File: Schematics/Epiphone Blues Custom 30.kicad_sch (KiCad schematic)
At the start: 280 parts, among them J3 Conn_Coaxial_Power, M1 Fan, SW2 EQ mode, SW3 POWER, SW5 PENTODE

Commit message: changed color of master volume
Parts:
- added A1: Arduino_UNO_R2, Module:Arduino_UNO_R2, symbol MCU_Module:Arduino_UNO_R2
- added D15: D, symbol Device:D
- added J10: Midi In, symbol Connector:DIN-5_180degree
- added M2: Servo, symbol Motor:Motor_Servo
- added R39: 220R, symbol Device:R
- added R54: 470R, symbol Device:R
- added R55: 1K, symbol Device:R
- added U1: 6N138, symbol Isolator:6N138
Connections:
- net at FCR.: now also B., C33.1, R49.1; no longer TRF4.
- net at 0VAC.: now also TR2.; no longer PT3.
- net at 60VAC.: now also TR2.; no longer PT11.
- net at PT2.: now also PT3., PT6. (x2)
- net at V7.: now also C29.1, R44.2, V6.
- net at PT5.: now also PT6. (x2)
- net at PT6.: no longer PT5. (x2)
- net at PT4.: now also PT1., PT7.
- net at ff.: now also BLUE.; no longer TR3.
- net at BLUE.: now also OT6.; no longer ff.
- net at PT7.: now also PT1.
- net at PT1.: no longer PT7.
- net at U?.: now also OUT1.; no longer TR3.
- net at OUT1.: now also PS1., V6.; no longer U?.
- net at 120VAC.: now also TR2.; no longer PT5.
- net at TR3.: now also d.; no longer d.
- net at a.: now also d.; no longer TR3.
- net at s.: now also d.; no longer TR3.
- net at d.: now also s.; no longer TR3.
- net at PT7.: now also 100VAC.
- net at 100VAC.: now also TR2.; no longer PT7.
- net at 5VAC.: now also PT13.
- net at PT13.: now also C35.1, HTFS., R50.1, V8.; no longer 5VAC.
- net at BLK.: now also SW3.; no longer PT1.
- net at SW3.: now also BLU.; no longer BLK.
- net at 0VAC.: now also TR2.; no longer PT6.
- net at 100VAC.: now also TR2.; no longer PT4.
- net at V6., V7.: now also PT15.; no longer PT14.
- net at PT1.: now also PT8.
- net at PT8.: no longer PT1.
- net at SW2.: now also RV7.; no longer RV5.
- net at RV7.: now also R23.2; no longer SW2.
- net at 120VAC.: now also TR2.; no longer PT8.
- net at PT2.: now also PT3.
- net at PT3.: no longer PT2.
- net at PT5.: now also PT1., PT8.
- net at 0VAC.: now also PT12.
- net at PT12.: now also F7.1; no longer 0VAC.
- net at s.: now also a.; no longer d.
- net at a.: now also J6., J7.; no longer s.
- net at BRN.: now also F9.2; no longer SW3.
- net at BLU.: now also AC-Input1.; no longer SW3.
- net at PT3.: now also PT2.
- net at PT2.: no longer PT3.
- new net: D6.1 (K), D7.1 (K), F., M1. (-), V1., V2., V3., V4., V5.
- new net: FCR., TRF4.
- new net: 0VAC., PT3.
- new net: 0VAC., TR2. (x2)
- new net: D4.2 (A), J4., RL3.
- new net: D3.2 (A), J4., RL1., RLY2.
- new net: J4., PB1.
- new net: 60VAC., PT11.
- new net: J3. (In), R29.1, RL3., V5A., V5B.
- new net: OUT2., PS2., V7.
- new net: TR3., ff.
- new net: TR3., U?.
- new net: B., PS5., PS6.
- new net: J5., J6., J7., J8., J9., d.
- new net: C4.2, RLY2., RV1.
- new net: 120VAC., PT5.
- new net: R19.2, RLY2., V2B.
- new net: RLY2., RV4.
- new net: TR3., d.
- new net: TR3., a.
- new net: TR3., s.
- new net: A1.15 (D0/RX), M2.1 (PWM)
- new net: A1.29 (GND), M2.3 (-), R55.2, U1.5 (GND)
- new net: A1.5 (+5V), M2.2 (+), R54.1, U1.8 (VCC)
- new net: BLK., PT1.
- new net: 0VAC., PT6.
- new net: 100VAC., PT4.
- new net: PT14., V6., V7.
- new net: C17.2, RV7., SW2.
- new net: RV5., SW2.
- new net: 120VAC., PT8.
- new net: R54.2, U1.6 (VO2)
- new net: D15.1 (K), R39.2, U1.2 (C1)
- new net: D15.2 (A), J10.5, U1.3 (C2)
- new net: C6.2, RL1., RV2., V1B.
- new net: BRN., SW3.
- new net: J2. (Ext), T1. (SA)
- new net: J10.4, R39.1
- new net: R55.1, U1.7 (VO1)
- now unconnected: PT1., PT1., PT3., PT3., PT6., PT6., PT7., PT8., V6., V6.
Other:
- note added: "Master volume is controlled by a servo motor. A MIDI expression pedal defines the rotation"
- moved on the sheet: 0VAC, 100VAC, 11.5VAC, 120VAC, 3.15VAC, 350VAC, 5VAC, 60VAC, A, AC-Input1, B, BLK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

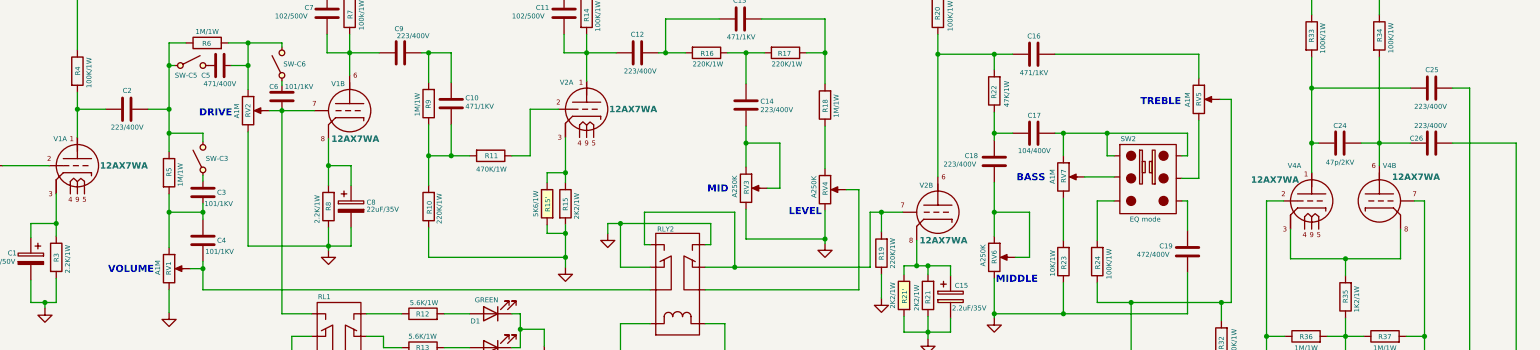
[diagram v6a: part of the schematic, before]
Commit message: Changed tube types in V1, V2 and V4
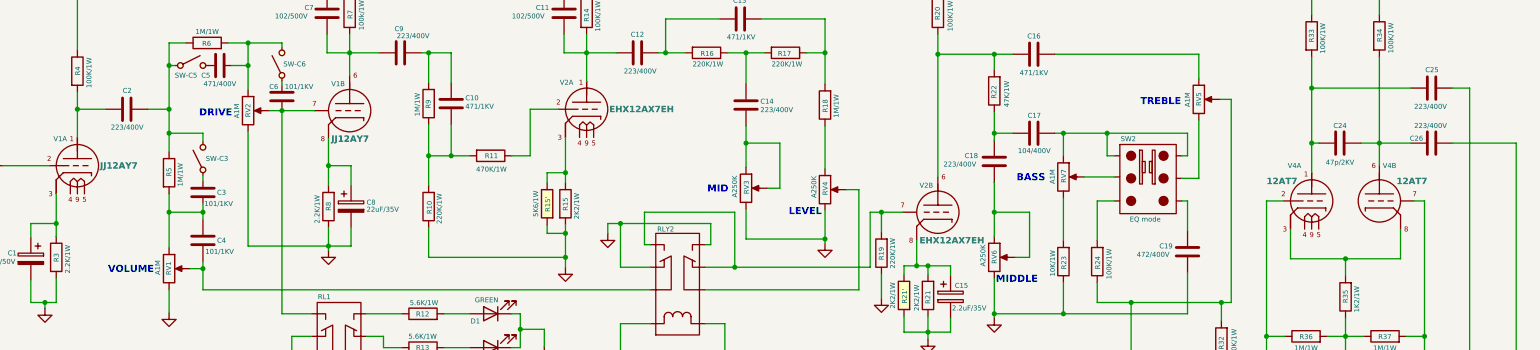
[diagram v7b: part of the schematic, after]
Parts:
- 0VAC, 100VAC, 11.5VAC, 120VAC, 3.15VAC, 350VAC, 5VAC, 60VAC, A, AC-Input1, B, BLK, BLU, BLUE, BRN, C, D, D10, D11, D12, D13, D14, D9, E, F, FCR, FCS, HTFR, HTFS, J1, J2, J4, J5, J6, J7, J8, J9, OTCT, OUT1, OUT2, PS1, PS2, PS3, PS4, PS5, PS6, PT1, PT10, PT11, PT12, PT13, PT14, PT15, PT2, PT3, PT4, PT5, PT6, PT7, PT8, PT9, RL1, RL3, RLY2, SS1, SS2, SW-C3, SW-C5, SW-C6, T1, V1, V2, V3, V4, V5, V6, V7, WHT: value ~ -> (none)
- V1A, V1B: value 12AX7WA -> JJ12AY7
- V2A, V2B: value 12AX7WA -> EHX12AX7EH
- V4A, V4B: value 12AX7WA -> 12AT7
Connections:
- net at FCR.: now also B., C33.1, R49.1; no longer TRF4.
- net at 0VAC.: now also TR2.; no longer PT3.
- net at 60VAC.: now also TR2.; no longer PT11.
- net at PT2.: now also PT3., PT6. (x2)
- net at V7.: now also C29.1, R44.2, V6.
- net at PT5.: now also PT6. (x2)
- net at PT6.: no longer PT5. (x2)
- net at PT4.: now also PT1., PT7.
- net at ff.: now also BLUE.; no longer TR3.
- net at BLUE.: now also OT6.; no longer ff.
- net at PT7.: now also PT1.
- net at PT1.: no longer PT7.
- net at U?.: now also OUT1.; no longer TR3.
- net at OUT1.: now also PS1., V6.; no longer U?.
- net at 120VAC.: now also TR2.; no longer PT5.
- net at TR3.: now also d.; no longer d.
- net at a.: now also d.; no longer TR3.
- net at s.: now also d.; no longer TR3.
- net at d.: now also s.; no longer TR3.
- net at PT7.: now also 100VAC.
- net at 100VAC.: now also TR2.; no longer PT7.
- net at 5VAC.: now also PT13.
- net at PT13.: now also C35.1, HTFS., R50.1, V8.; no longer 5VAC.
- net at BLK.: now also SW3.; no longer PT1.
- net at SW3.: now also BLU.; no longer BLK.
- net at 0VAC.: now also TR2.; no longer PT6.
- net at 100VAC.: now also TR2.; no longer PT4.
- net at V6., V7.: now also PT15.; no longer PT14.
- net at PT1.: now also PT8.
- net at PT8.: no longer PT1.
- net at SW2.: now also RV7.; no longer RV5.
- net at RV7.: now also R23.2; no longer SW2.
- net at 120VAC.: now also TR2.; no longer PT8.
- net at PT2.: now also PT3.
- net at PT3.: no longer PT2.
- net at PT5.: now also PT1., PT8.
- net at 0VAC.: now also PT12.
- net at PT12.: now also F7.1; no longer 0VAC.
- net at s.: now also a.; no longer d.
- net at a.: now also J6., J7.; no longer s.
- net at BRN.: now also F9.2; no longer SW3.
- net at BLU.: now also AC-Input1.; no longer SW3.
- net at PT3.: now also PT2.
- net at PT2.: no longer PT3.
- new net: D6.1 (K), D7.1 (K), F., M1. (-), V1., V2., V3., V4., V5.
- new net: FCR., TRF4.
- new net: 0VAC., PT3.
- new net: 0VAC., TR2. (x2)
- new net: D4.2 (A), J4., RL3.
- new net: D3.2 (A), J4., RL1., RLY2.
- new net: J4., PB1.
- new net: 60VAC., PT11.
- new net: J3. (In), R29.1, RL3., V5A., V5B.
- new net: OUT2., PS2., V7.
- new net: TR3., ff.
- new net: TR3., U?.
- new net: B., PS5., PS6.
- new net: J5., J6., J7., J8., J9., d.
- new net: C4.2, RLY2., RV1.
- new net: 120VAC., PT5.
- new net: R19.2, RLY2., V2B.
- new net: RLY2., RV4.
- new net: TR3., d.
- new net: TR3., a.
- new net: TR3., s.
- new net: BLK., PT1.
- new net: 0VAC., PT6.
- new net: 100VAC., PT4.
- new net: PT14., V6., V7.
- new net: C17.2, RV7., SW2.
- new net: RV5., SW2.
- new net: 120VAC., PT8.
- new net: C6.2, RL1., RV2., V1B.
- new net: BRN., SW3.
- new net: J2. (Ext), T1. (SA)
- now unconnected: PT1., PT1., PT3., PT3., PT6., PT6., PT7., PT8., V6., V6.
